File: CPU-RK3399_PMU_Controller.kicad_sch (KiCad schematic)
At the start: 1 part

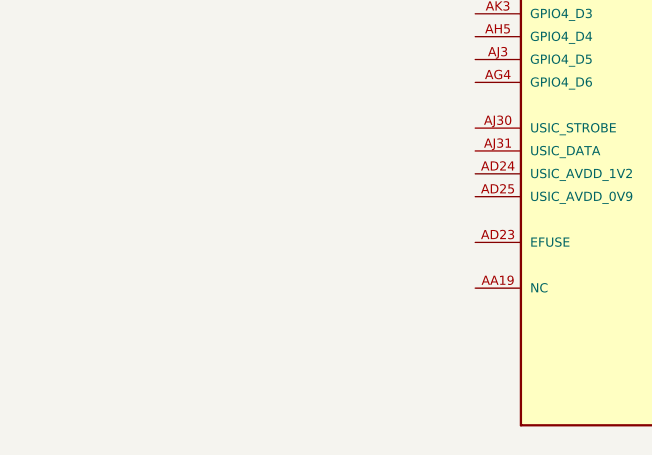
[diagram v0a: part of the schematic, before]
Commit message: update RK3399 power
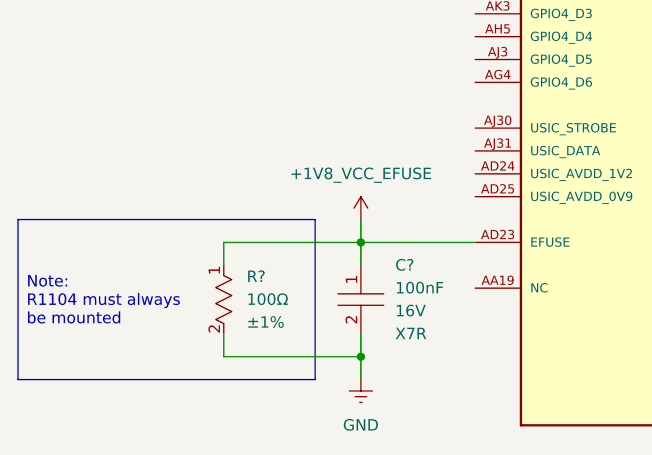
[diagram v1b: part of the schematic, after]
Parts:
- added C?: ~, footprints:CAPC1005X50N, symbol component_library:Capacitors/CL05B104KO5NNNC
- added R?: ~, footprints:RESC1005X35N, symbol component_library:Resistors/0402WGF1000TCE
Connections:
- net +1V8_VCC_EFUSE: now reaches U?.AD23 (EFUSE)
- net +1V8_VCC_EFUSE: now also C?.1, R?.1
- new net GND: C?.2, R?.2

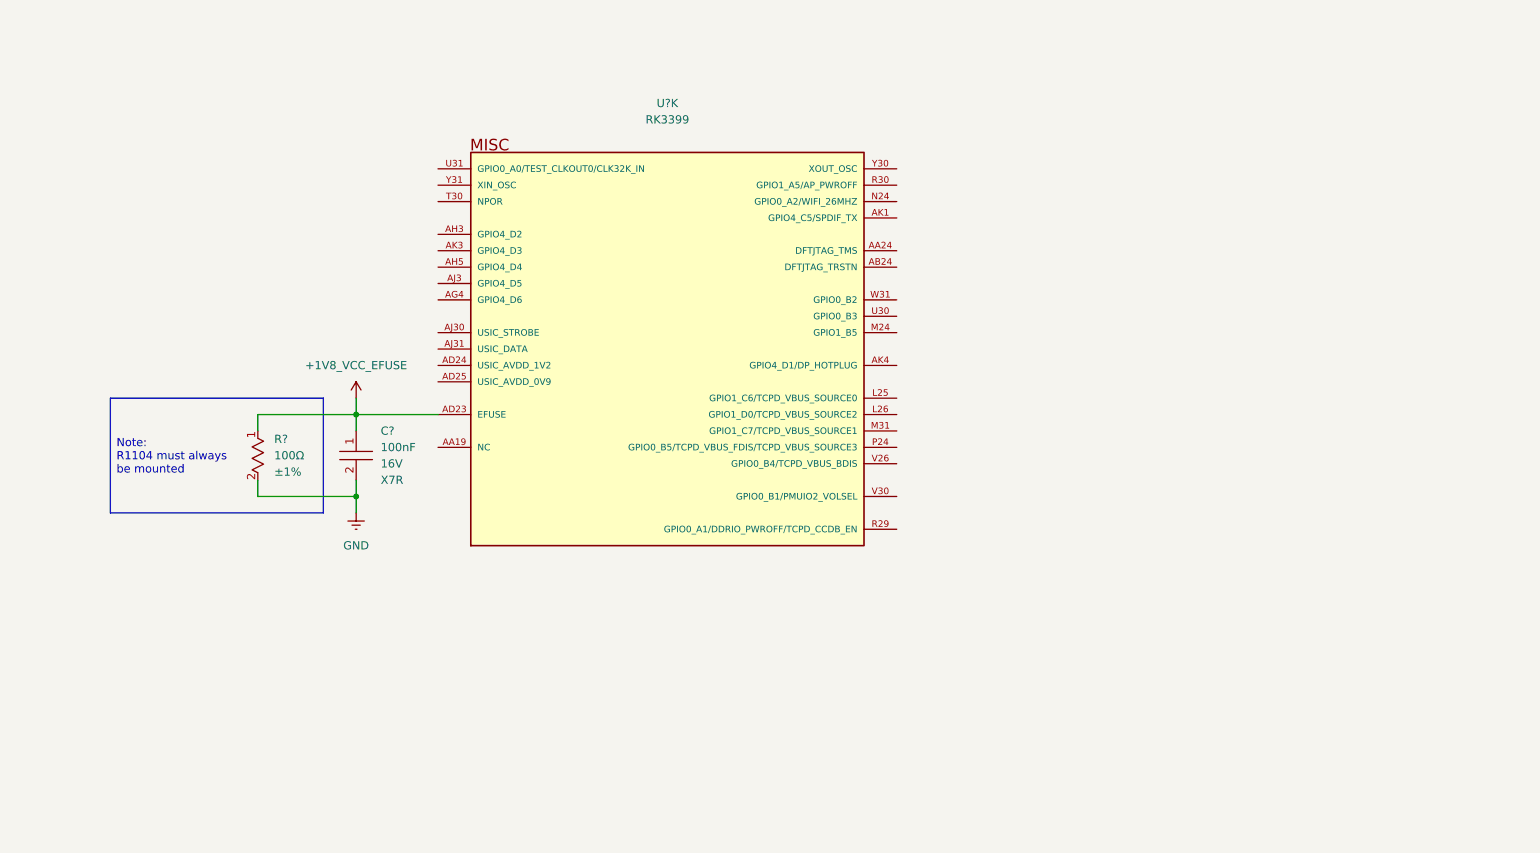
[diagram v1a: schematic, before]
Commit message: design CPU DDR
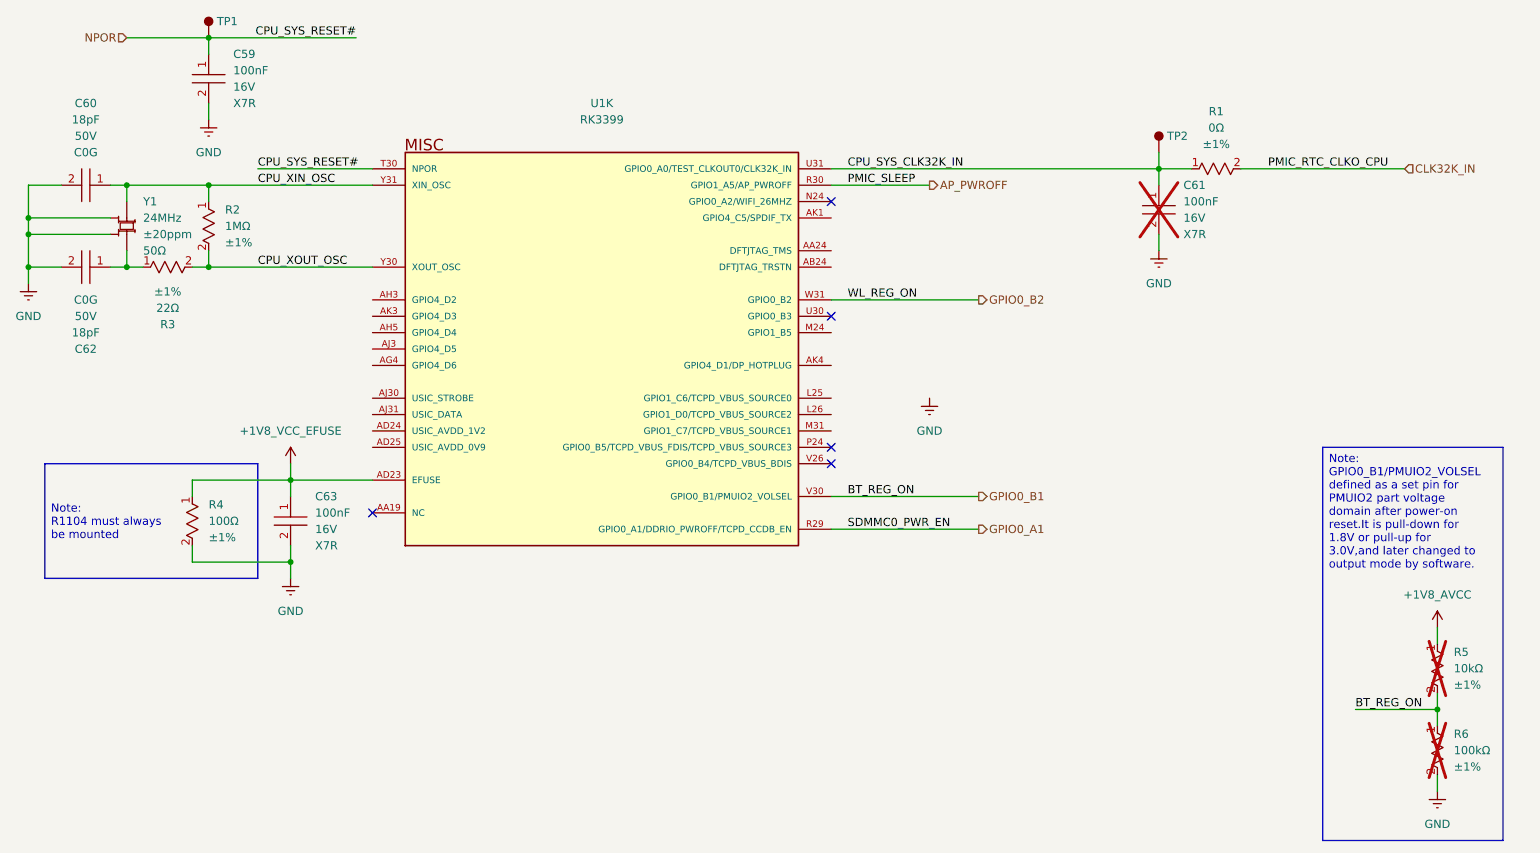
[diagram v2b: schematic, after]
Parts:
- removed C?: ~, footprints:CAPC1005X50N, symbol component_library:Capacitors/CL05B104KO5NNNC
- removed R?: ~, footprints:RESC1005X35N, symbol component_library:Resistors/0402WGF1000TCE
- added C59, C61, C63: ~, footprints:CAPC1005X50N, symbol component_library:Capacitors/CL05B104KO5NNNC
- added C60, C62: ~, footprints:CAPC1005X50N, symbol component_library:Capacitors/0402CG180J500NT
- added R1: ~, footprints:RESC1005X35N, symbol component_library:Resistors/0402WGF0000TCE
- added R2: ~, footprints:RESC1005X35N, symbol component_library:Resistors/0402WGF1004TCE
- added R3: ~, footprints:RESC1005X35N, symbol component_library:Resistors/0402WGF220JTCE
- added R4: ~, footprints:RESC1005X35N, symbol component_library:Resistors/0402WGF1000TCE
- added R5: ~, footprints:RESC1005X35N, symbol component_library:Resistors/0402WGF1002TCE
- added R6: ~, footprints:RESC1005X35N, symbol component_library:Resistors/0402WGF1003TCE
- added TP1, TP2: ~, footprints:, symbol component_library:Mechanical/Test_Point
- added Y1: ~, footprints:, symbol component_library:Crystals, Oscillators, Resonators/X322524MOB4SI
- gave numbers to parts that had none: 1
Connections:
- net +1V8_VCC_EFUSE: now also C63.1, R4.1
- net GND: now also C59.2, C60.2, C61.2, C62.2, C63.2, R4.2, R6.2, Y1.2, Y1.4
- net GPIO0_A1: now reaches U1.R29 (GPIO0_A1/DDRIO_PWROFF/TCPD_CCDB_EN)
- net AP_PWROFF: now reaches U1.R30 (GPIO1_A5/AP_PWROFF)
- net NPOR: now reaches U1.T30 (NPOR)
- net NPOR: now also C59.1, TP1.TP
- net CPU_SYS_CLK32K_IN: now reaches U1.U31 (GPIO0_A0/TEST_CLKOUT0/CLK32K_IN)
- net CPU_SYS_CLK32K_IN: now also C61.1, R1.1, TP2.TP
- net GPIO0_B1: now reaches U1.V30 (GPIO0_B1/PMUIO2_VOLSEL)
- net GPIO0_B1: now also R5.2, R6.1
- net GPIO0_B2: now reaches U1.W31 (GPIO0_B2)
- net CPU_XOUT_OSC: now reaches U1.Y30 (XOUT_OSC)
- net CPU_XOUT_OSC: now also R2.2, R3.2
- net CPU_XIN_OSC: now reaches U1.Y31 (XIN_OSC)
- net CPU_XIN_OSC: now also C60.1, R2.1, Y1.1
- new net: C62.1, R3.1, Y1.3
- new net +1V8_AVCC: R5.1
- new net CLK32K_IN: R1.2
- no-connect marks 0 -> 5
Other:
- moved on the sheet: U1K

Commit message: design CPU-RK3399 eMMC Controller
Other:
- company: (none) -> TickLab
- title: (none) -> CPU-RK3399 PMU
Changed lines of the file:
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@@
 	(paper "A4")
 	(title_block
-		(date "2026-01-09")
+		(title "CPU-RK3399 PMU")
+		(date "2026-01-14")
 		(rev "1.0.0")
+		(company "TickLab")
 	)
 	(text_box "Note:\nR1104 must always\nbe mounted"

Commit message: design USB
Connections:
- no-connect marks 5 -> 9
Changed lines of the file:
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@@
+	)
+	(no_connect
+		(at 104.14 99.06)
+	)
+	(no_connect
+		(at 104.14 96.52)
 	)
 	(no_connect
@@
 	)
 	(no_connect
+		(at 104.14 91.44)
+	)
+	(no_connect
+		(at 104.14 93.98)
+	)
+	(no_connect
